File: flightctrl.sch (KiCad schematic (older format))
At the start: 53 parts, among them J1 USB_OTG, P1 CONN_02X03, SW1 SW_SPST, SW10 ROTARY_ENCODER_SWITCH, SW2 SW_SPST, SW3 SW_SPST, SW4 SW_SPST, SW5 SW_SPDT_MSM, SW6 ROTARY_ENCODER_SWITCH, SW7 ROTARY_ENCODER_SWITCH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

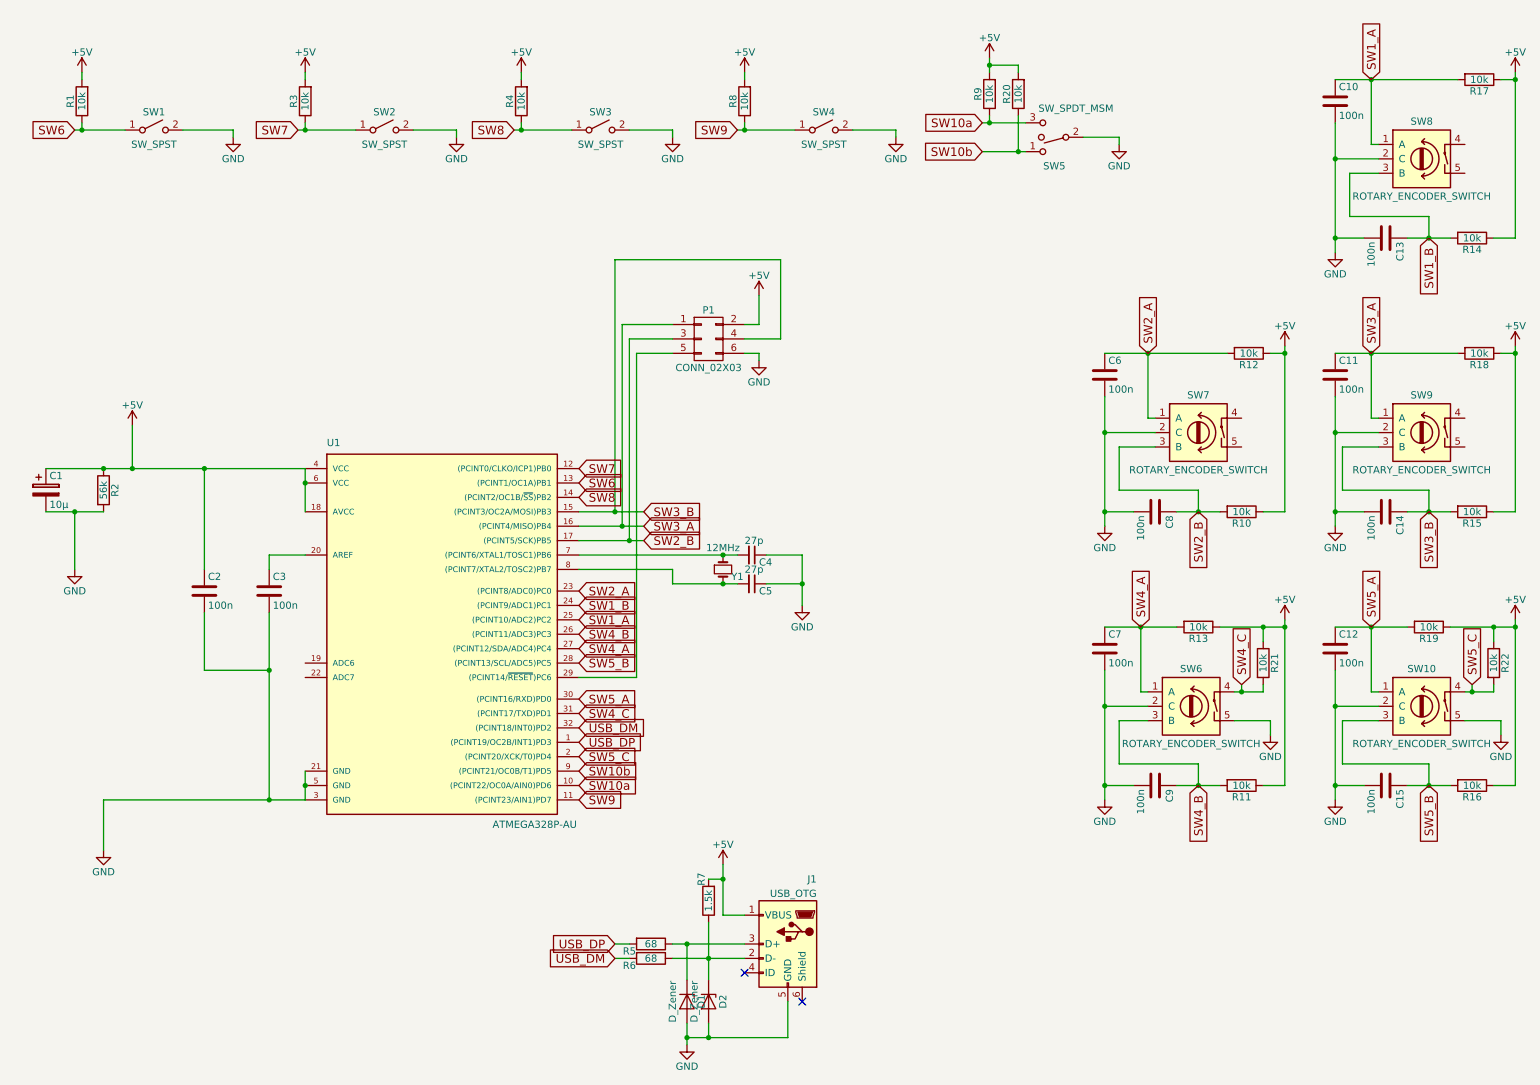
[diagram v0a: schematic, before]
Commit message: create new hardware schematic and layout
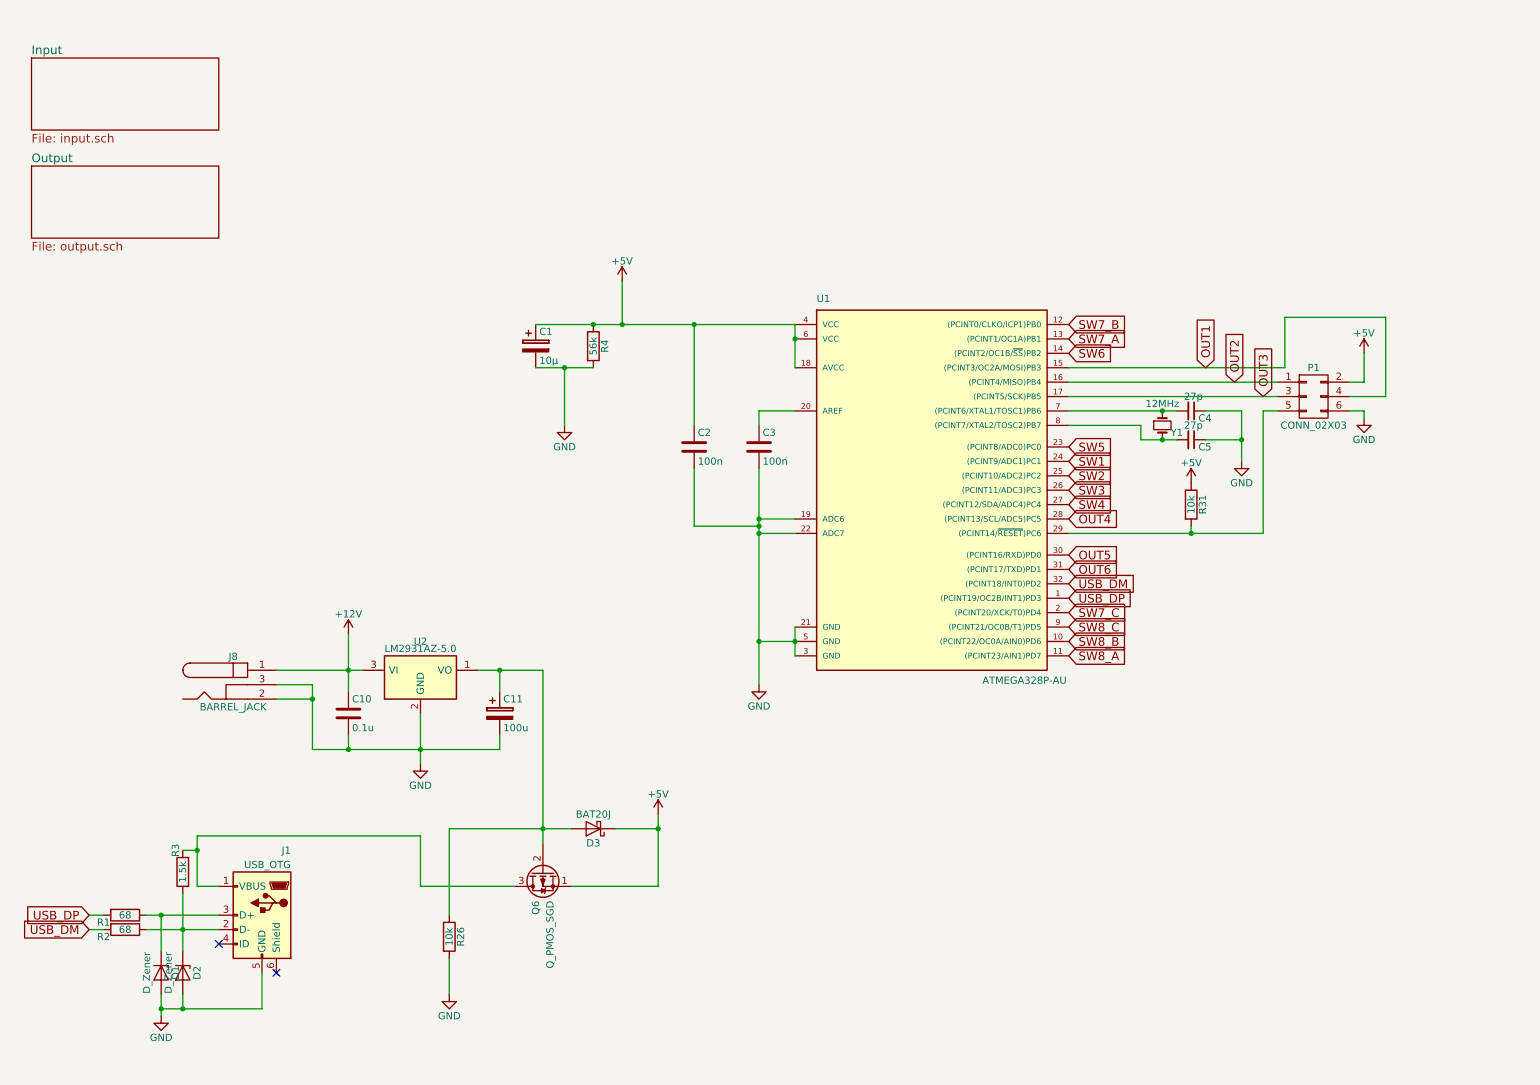
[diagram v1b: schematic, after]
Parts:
- removed C11, C12, C13, C14, C15, C6, C7, C8, C9: 100n, Capacitors_SMD:C_0805, symbol C
- removed R1, R10, R11, R12, R13, R14, R15, R16, R17, R18, R19, R20, R21, R22, R3, R4, R8, R9: 10k, Resistors_SMD:R_0805, symbol R
- removed SW1, SW2, SW3, SW4: SW_SPST, Button_Switch_THT:MKIP1PUM, symbol SW_SPST
- removed SW10, SW6, SW7, SW8, SW9: ROTARY_ENCODER_SWITCH, Button_Switch_THT:PEC11R-4xxxF-Sxxx, symbol Rotary_Encoder_Switch
- removed SW5: SW_SPDT_MSM, Button_Switch_THT:MKIP1PUM, symbol SW_SPDT_MSM
- added C11: 100u, Capacitors_ThroughHole:CP_Radial_D4.0mm_P2.00mm, symbol CP
- added D3: BAT20J, Diodes_SMD:D_SOD-323, symbol D_Schottky
- added J8: BARREL_JACK, Connect:BARREL_JACK, symbol BARREL_JACK
- added Q6: Q_PMOS_SGD, TO_SOT_Packages_THT:TO-92_Rugged, symbol Q_PMOS_SGD
- added R26: 10k, Resistors_SMD:R_0805, symbol R
- added R31: 10k, Resistors_ThroughHole:R_Axial_DIN0204_L3.6mm_D1.6mm_P7.62mm_Horizontal, symbol R
- added U2: LM2931AZ-5.0, TO_SOT_Packages_THT:TO-92_Rugged, symbol LM2931AZ-5.0
- C1: footprint Capacitors_ThroughHole:C_Radial_D5_L11_P2 -> Capacitors_ThroughHole:CP_Radial_D5.0mm_P2.00mm
- C10: value 100n -> 0.1u
- P1: footprint Pin_Headers:Pin_Header_Straight_2x03 -> Pin_Headers:Pin_Header_Straight_2x03_Pitch2.54mm
- renumbered R5 to R1, R6 to R2, R7 to R3, R2 to R4
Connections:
- net SW8 is gone; now on net SW6: U1.14 ((PCINT2/OC1B/~SS~)PB2)
- net +5V: now also D3.1 (K), Q6.1 (S), R31.1; no longer J1.1 (VBUS), R3.2
- net GND: now also U1.19 (ADC6), U1.22 (ADC7), C11.2, J8.2, J8.3, R26.2, U2.2 (GND)
- net SW6: no longer U1.13 ((PCINT1/OC1A)PB1)
- net at P1.5 (P5), U1.29 ((PCINT14/~RESET~)PC6): now also R31.2
- net SW10a renamed SW8_B
- net SW10b renamed SW8_C
- net SW1_A renamed +12V
- net +12V: now also J8.1, U2.3 (VI); no longer U1.25 ((PCINT10/ADC2)PC2)
- net SW1_B renamed SW1
- net SW2_A renamed SW5
- net SW2_B renamed OUT3
- net SW3_A renamed OUT2
- net SW3_B renamed OUT1
- net SW4_A renamed SW4
- net SW4_B renamed SW3
- net SW4_C renamed OUT6
- net SW5_A renamed OUT5
- net SW5_B renamed OUT4
- net SW5_C renamed SW7_C
- net SW7 renamed SW7_B
- net SW9 renamed SW8_A
- new net: J1.1 (VBUS), Q6.3 (D), R3.2
- new net: C11.1, D3.2 (A), Q6.2 (G), R26.1, U2.1 (VO)
- new net SW2: U1.25 ((PCINT10/ADC2)PC2)
- new net SW7_A: U1.13 ((PCINT1/OC1A)PB1)
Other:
- moved on the sheet: C1, C2, C3, C4, C5, D1, D2, J1, P1, R1, R2, R3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

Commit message: update project for KiCAD 5.0, recreate/fix PCB
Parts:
- C1: footprint Capacitors_ThroughHole:CP_Radial_D5.0mm_P2.00mm -> Capacitor_THT:CP_Radial_D5.0mm_P2.00mm; symbol CP -> flightctrl-rescue:CP
- C10, C2, C3: footprint Capacitors_SMD:C_0805 -> Capacitor_SMD:C_0805_2012Metric; symbol C -> flightctrl-rescue:C
- C11: footprint Capacitors_ThroughHole:CP_Radial_D4.0mm_P2.00mm -> Capacitor_THT:CP_Radial_D4.0mm_P2.00mm; symbol CP -> flightctrl-rescue:CP
- C4, C5: footprint Capacitors_SMD:C_0805 -> Capacitor_SMD:C_0805_2012Metric; symbol C_Small -> flightctrl-rescue:C_Small
- D1, D2: footprint Diodes_SMD:D_MiniMELF -> Diode_SMD:D_MiniMELF; symbol D_Zener -> flightctrl-rescue:D_Zener
- D3: footprint Diodes_SMD:D_SOD-323 -> Diode_SMD:D_SOD-323; symbol D_Schottky -> flightctrl-rescue:D_Schottky
- J1: symbol USB_OTG -> flightctrl-rescue:USB_OTG
- J8: footprint Connect:BARREL_JACK -> Connector_BarrelJack:BarrelJack_Horizontal; symbol BARREL_JACK -> flightctrl-rescue:BARREL_JACK
- P1: footprint Pin_Headers:Pin_Header_Straight_2x03_Pitch2.54mm -> Connector_PinHeader_2.54mm:PinHeader_2x03_P2.54mm_Vertical; symbol CONN_02X03 -> flightctrl-rescue:CONN_02X03
- Q6: footprint TO_SOT_Packages_THT:TO-92_Rugged -> Package_TO_SOT_THT:TO-92_HandSolder; symbol Q_PMOS_SGD -> flightctrl-rescue:Q_PMOS_SGD
- R1, R2, R26, R3, R4: footprint Resistors_SMD:R_0805 -> Resistor_SMD:R_0805_2012Metric; symbol R -> flightctrl-rescue:R
- R31: footprint Resistors_ThroughHole:R_Axial_DIN0204_L3.6mm_D1.6mm_P7.62mm_Horizontal -> Resistor_THT:R_Axial_DIN0204_L3.6mm_D1.6mm_P7.62mm_Horizontal; symbol R -> flightctrl-rescue:R
- U1: footprint Housings_QFP:TQFP-32_7x7mm_Pitch0.8mm -> Package_QFP:TQFP-32_7x7mm_P0.8mm; symbol ATMEGA328P-AU -> flightctrl-rescue:ATMEGA328P-AU
- U2: footprint TO_SOT_Packages_THT:TO-92_Rugged -> Package_TO_SOT_THT:TO-92_HandSolder; symbol LM2931AZ-5.0 -> flightctrl-rescue:LM2931AZ-5.0
- Y1: footprint Crystals:Crystal_SMD_HC49-SD -> Crystal:Crystal_SMD_HC49-SD; symbol Crystal_Small -> flightctrl-rescue:Crystal_Small
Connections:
- net SW7_A: now also U1.12 ((PCINT0/CLKO/ICP1)PB0); no longer U1.13 ((PCINT1/OC1A)PB1)
- net SW7_B: now also U1.13 ((PCINT1/OC1A)PB1); no longer U1.12 ((PCINT0/CLKO/ICP1)PB0)
- net SW8_A: now also U1.10 ((PCINT22/OC0A/AIN0)PD6); no longer U1.11 ((PCINT23/AIN1)PD7)
- net SW8_B: now also U1.11 ((PCINT23/AIN1)PD7); no longer U1.10 ((PCINT22/OC0A/AIN0)PD6)
